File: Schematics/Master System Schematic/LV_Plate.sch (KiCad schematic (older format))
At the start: 0 parts

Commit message: LV Plate
> Added basic connectors and outlines for MCR PCB
> Added and wired components on LV Plate
> Added GLV connector
> Connected layers
> Some wire gauges still needed

LV_Plate Version 1.0
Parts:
- added U?: OrionBMS2, symbol NER:OrionBMS2
- added U?: Bender_Isometer_IR155-3204, symbol NER:Bender_Isometer_IR155-3204
- added U?: OrionThermExp, symbol NER:OrionThermExp
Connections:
- new net BMS_Fault: U?.26 (MP_En)
- new net Charge_Safety: U?.6 (Charge_Safety)
- new net HV_Sense+: U?.~ (STATUS_OK)
- new net HV_Sense-: U?.~ (STATUS_OK)
- new net IMD_Fault: U?.~ (STATUS_OK)
- new net IMD_GND1: U?.~ (STATUS_OK)
- new net IMD_GND2: U?.~ (STATUS_OK)
- new net MCR_PCB/BMS_C_12V: U?.3 (RM2+)
- new net MCR_PCB/BMS_GND: U?.12 (GND)
- new net MCR_PCB/BMS_R_12V: U?.2 (RM1-)
- new net MCR_PCB/IMD_12V: U?.~ (STATUS_OK)
- new net MCR_PCB/IMD_GND: U?.~ (STATUS_OK)
- new net MCR_PCB/Therm_12V: U?.2 (PowerA)
- new net MCR_PCB/Therm_GND: U?.4 (GND)
- no-connect marks 0 -> 27
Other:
- note added: "Therm Cutout"
- note added: "VT Cutout"

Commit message: LV Plate Cleanup + Other Small Stuff
> Renamed MCR PCB to BattBox PCB
> Added 7 Pin IMD connector to BattBox PCB
> Fixed wire gauges on Segment Layer sheet
> Added HV cutout on LV Plate
> Added fan signals
> Deleted old accumulator stuff
> Added BattBox and BMS fans

BattBox PCB V1.0
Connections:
- net IMD_Fault: no longer U?.~ (STATUS_OK)
- net RadFan: now reaches U?.10 (MPOut3/Fan_En)
- net BMSFanSig: now reaches U?.15
- net BattFanPWM: now reaches U?.24 (MPOut4/Fan_PWM)
- new net MCR_PCB/IMD_Fault_IN: U?.~ (STATUS_OK)
- no-connect marks 27 -> 26
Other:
- note added: "GLV Conn Cutout"
- note added: "HV Cutout"

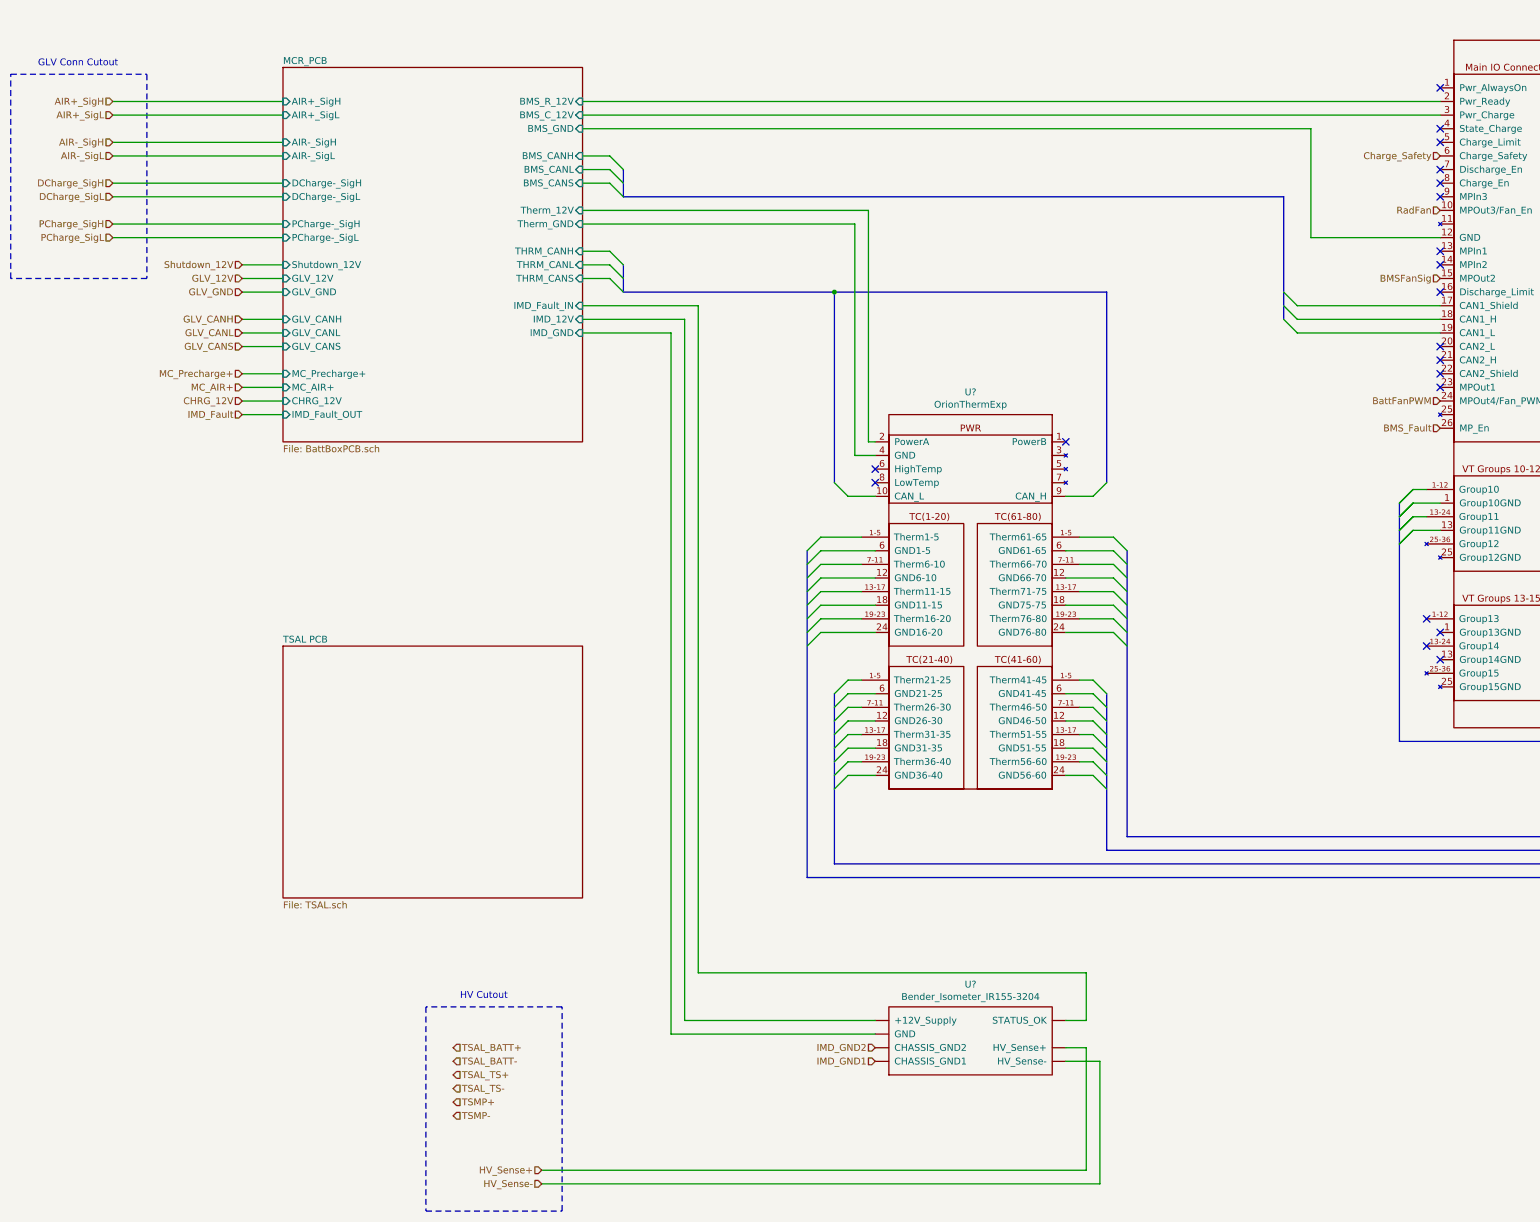
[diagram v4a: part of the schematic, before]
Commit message: LV Plate and VPM board
Verified and updated LV plate connections
Setup VPM board stand-in
Organized main battery box schematic
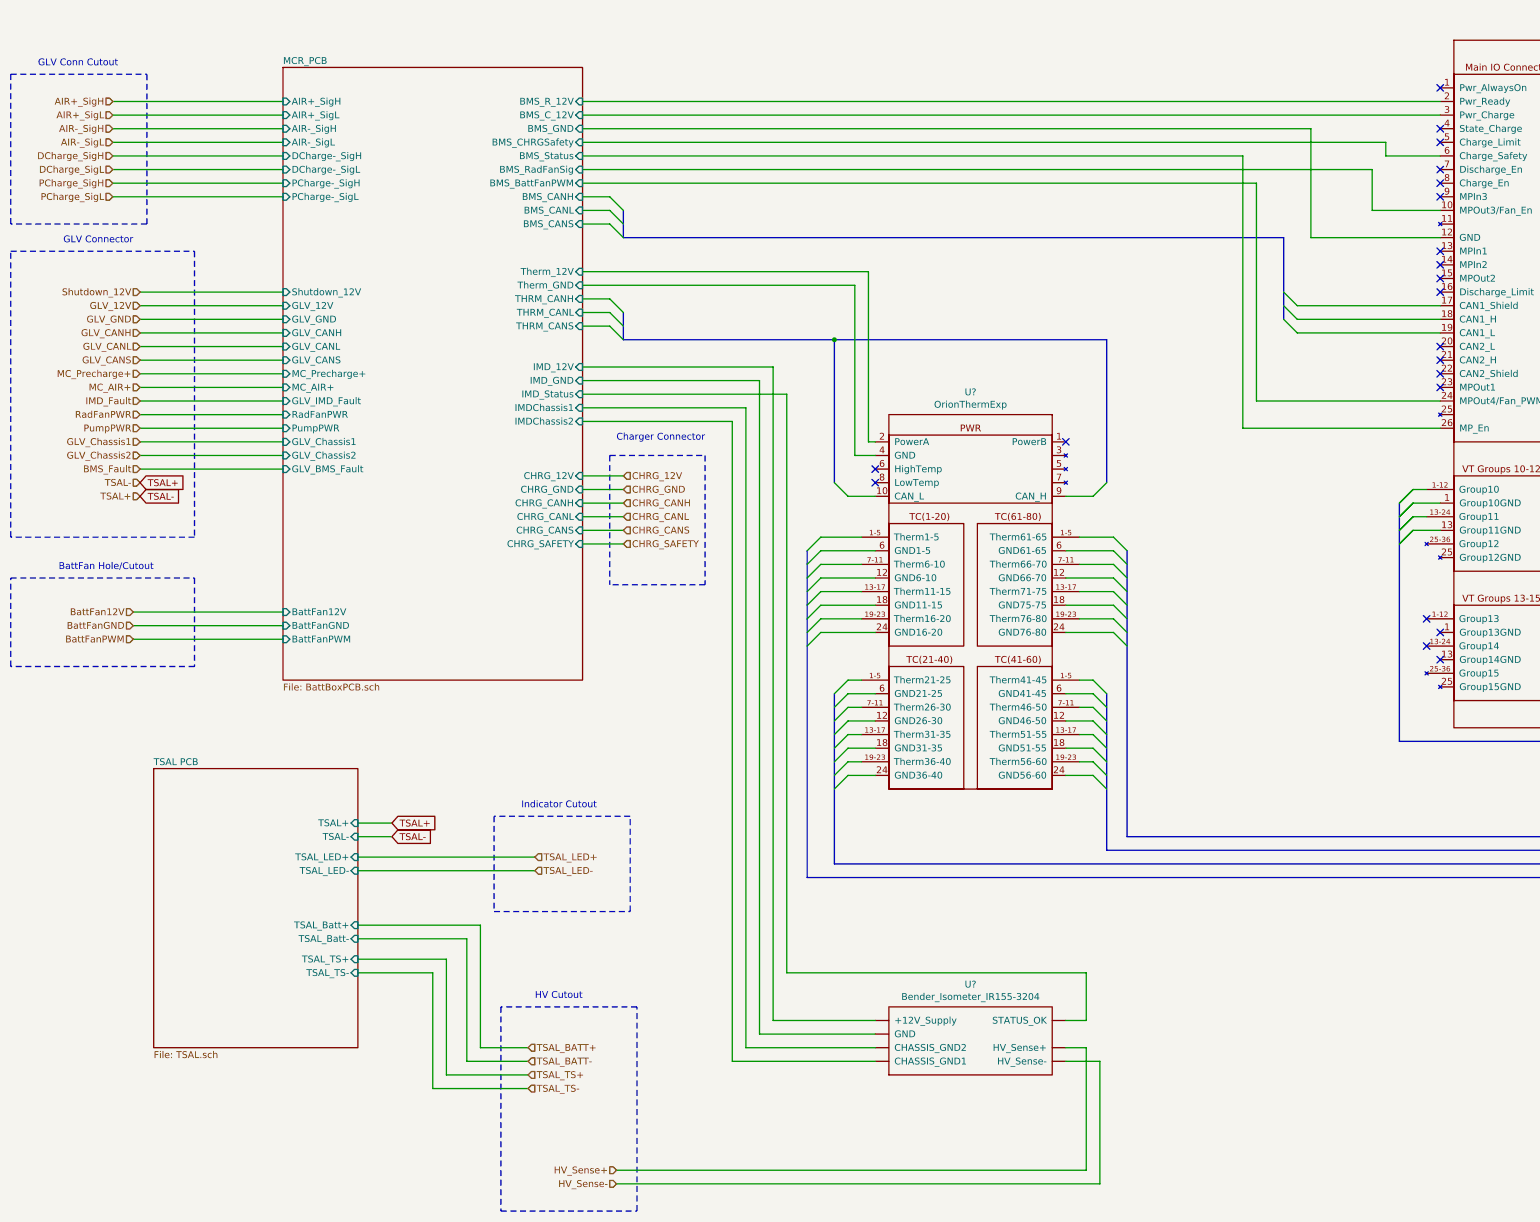
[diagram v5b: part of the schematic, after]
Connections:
- net IMD_GND2 is gone; now on net MCR_PCB/IMD_Status: U?.~ (STATUS_OK)
- net MCR_PCB/IMD_Fault_IN is gone; now on net MCR_PCB/IMD_Status: U?.~ (STATUS_OK)
- net BMS_Fault: no longer U?.26 (MP_En)
- net BattFanPWM: no longer U?.24 (MPOut4/Fan_PWM)
- removed net BMSFanSig: U?.15
- net Charge_Safety renamed MCR_PCB/BMS_CHRGSafety
- net IMD_GND1 renamed MCR_PCB/IMD_Status
- net RadFan renamed MCR_PCB/BMS_RadFanSig
- new net MCR_PCB/BMS_BattFanPWM: U?.24 (MPOut4/Fan_PWM)
- new net MCR_PCB/BMS_Status: U?.26 (MP_En)
- new net MCR_PCB/IMDChassis1: U?.~ (STATUS_OK)
- new net MCR_PCB/IMDChassis2: U?.~ (STATUS_OK)
- no-connect marks 26 -> 27
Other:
- note added: "BattFan Hole/Cutout"
- note added: "Charger Connector\n"
- note added: "GLV Connector"
- note added: "Indicator Cutout"

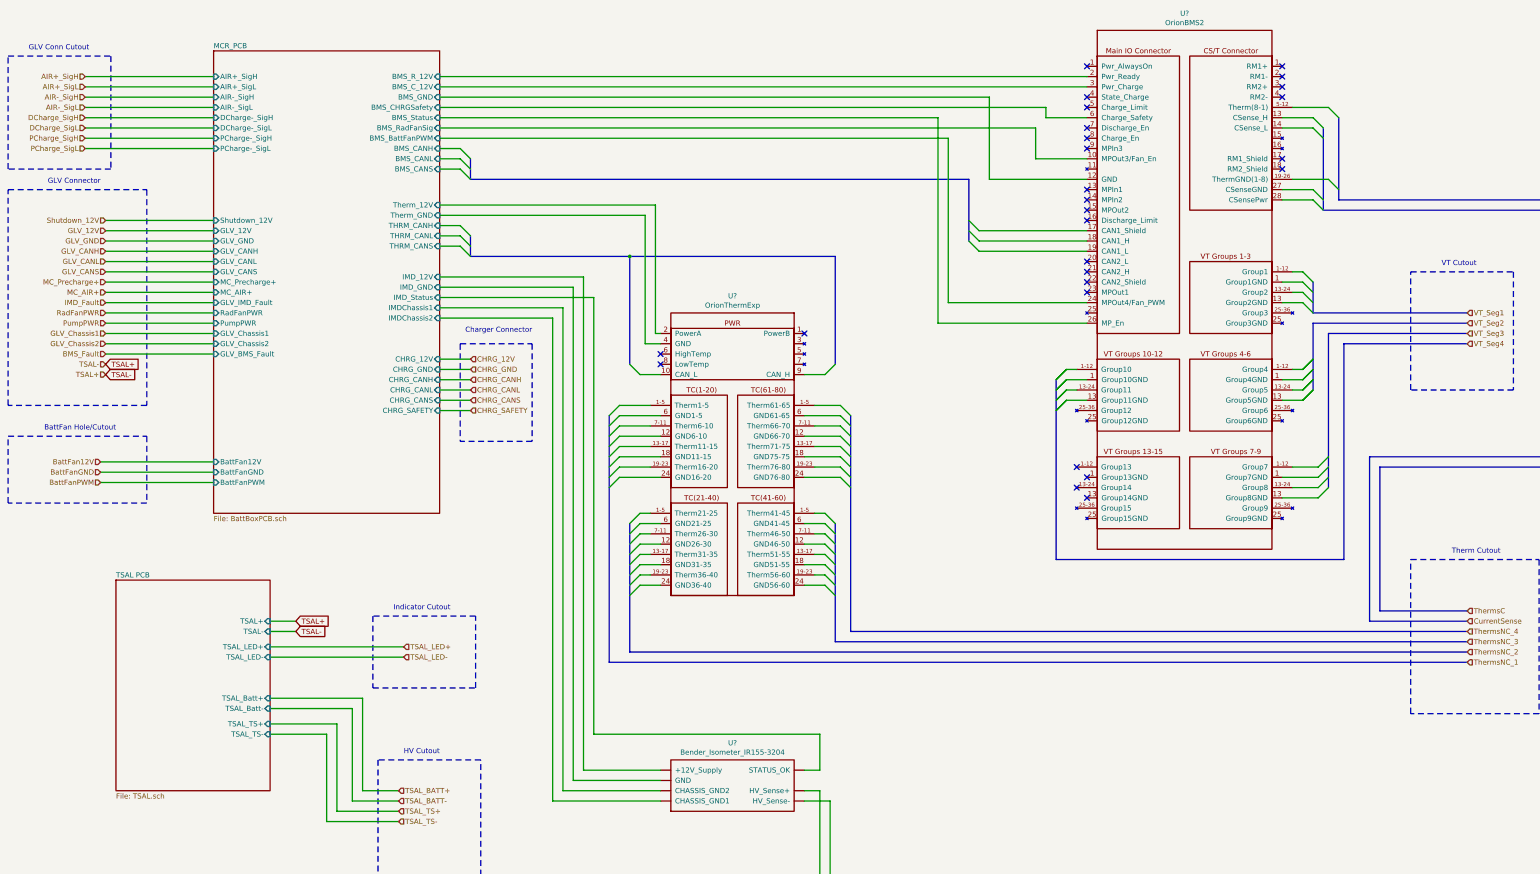
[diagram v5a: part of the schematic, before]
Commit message: Battbox and master update
- Fixed all connections within battbox and did some formatting
- Added all battbox connections to master
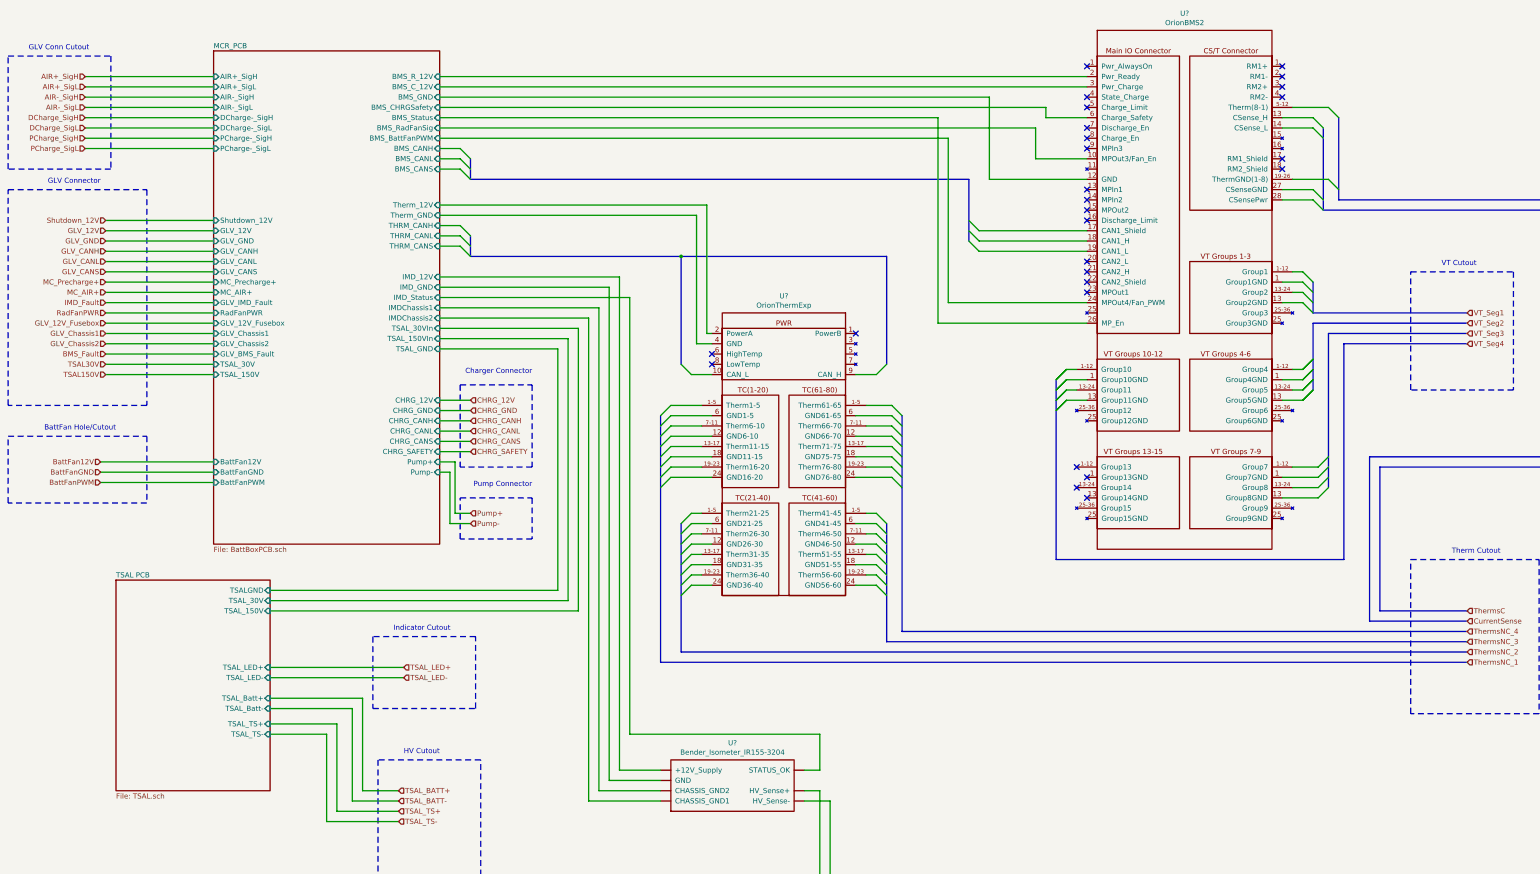
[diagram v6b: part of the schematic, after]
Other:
- note added: "Pump Connector\n"
- moved on the sheet: U?

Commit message: Annotations complete
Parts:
- gave numbers to parts that had none: 3
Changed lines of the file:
@@
 EESchema Schematic File Version 4
+LIBS:Master System Schematic-cache
 EELAYER 30 0
 EELAYER END
@@
 AR Path="/626EC638/61396B9E" Ref="U?"  Part="1"
 AR Path="/5F45B05E/60827CB0/61396B9E" Ref="U?"  Part="1"
-AR Path="/60C39CCE/60827CB0/61396B9E" Ref="U?"  Part="1"
-F 0 "U?" H 7850 8865 50  0000 C CNN
+AR Path="/60C39CCE/60827CB0/61396B9E" Ref="U2201"  Part="1"
+F 0 "U2201" H 7850 8865 50  0000 C CNN
 F 1 "Bender_Isometer_IR155-3204" H 7850 8774 50  0000 C CNN
 F 2 "" H 7850 8750 50  0001 C CNN
@@
 AR Path="/60D53BFB/613916C2" Ref="U?"  Part="1"
 AR Path="/5F45B05E/60827CB0/613916C2" Ref="U?"  Part="1"
-AR Path="/60C39CCE/60827CB0/613916C2" Ref="U?"  Part="1"
-F 0 "U?" H 12250 4265 50  0000 C CNN
+AR Path="/60C39CCE/60827CB0/613916C2" Ref="U2203"  Part="1"
+F 0 "U2203" H 12250 4265 50  0000 C CNN
 F 1 "OrionBMS2" H 12250 4174 50  0000 C CNN
 F 2 "" H 12250 4200 50  0001 C CNN
@@
 AR Path="/5F45B05E/61399F97" Ref="U?"  Part="1"
 AR Path="/5F45B05E/60827CB0/61399F97" Ref="U?"  Part="1"
-AR Path="/60C39CCE/60827CB0/61399F97" Ref="U?"  Part="1"
-F 0 "U?" H 8350 4615 50  0000 C CNN
+AR Path="/60C39CCE/60827CB0/61399F97" Ref="U2202"  Part="1"
+F 0 "U2202" H 8350 4615 50  0000 C CNN
 F 1 "OrionThermExp" H 8350 4524 50  0000 C CNN
 F 2 "" H 8350 4350 50  0001 C CNN
